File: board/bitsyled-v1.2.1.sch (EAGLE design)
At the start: 8 parts

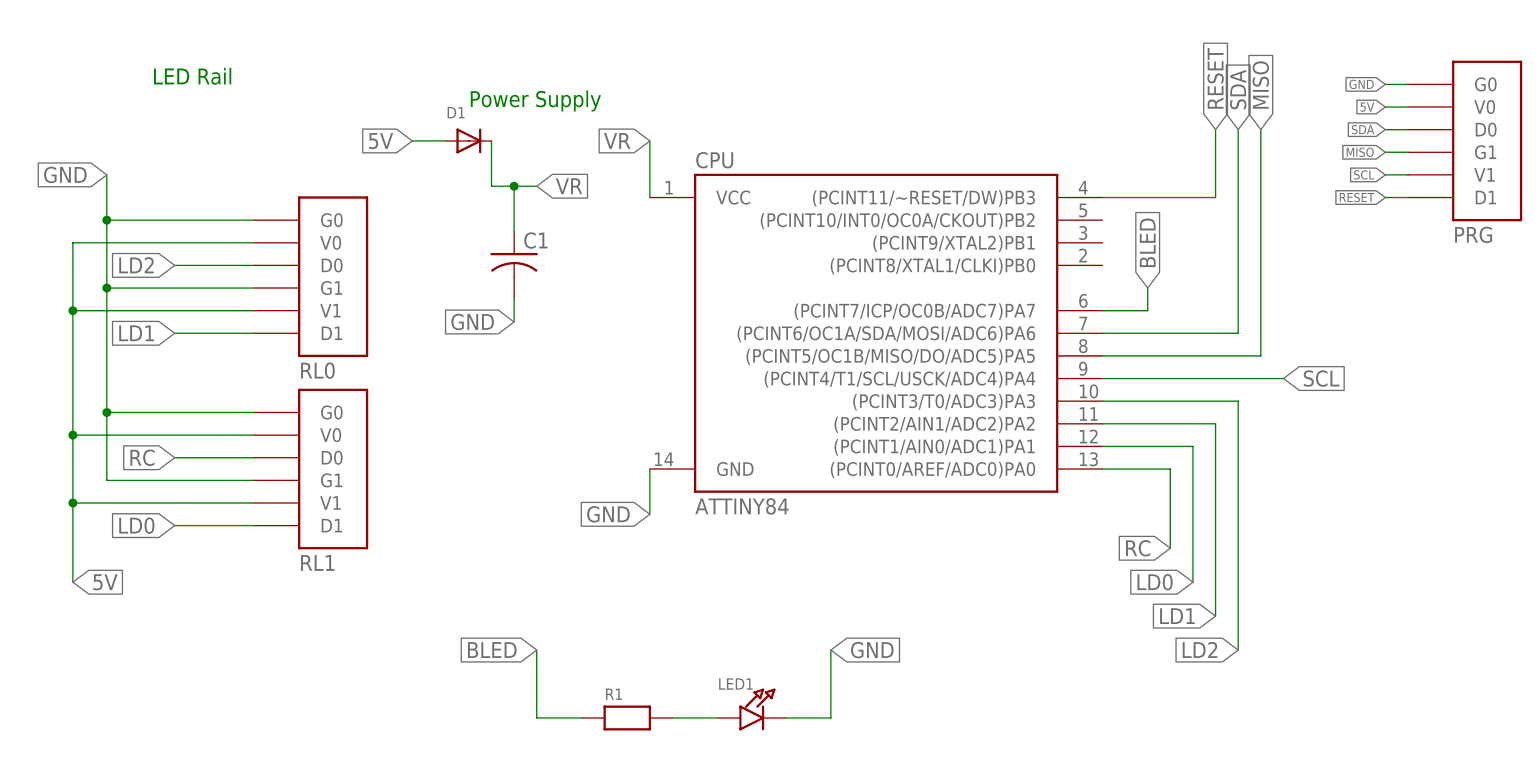
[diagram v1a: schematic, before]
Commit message: Adding presets
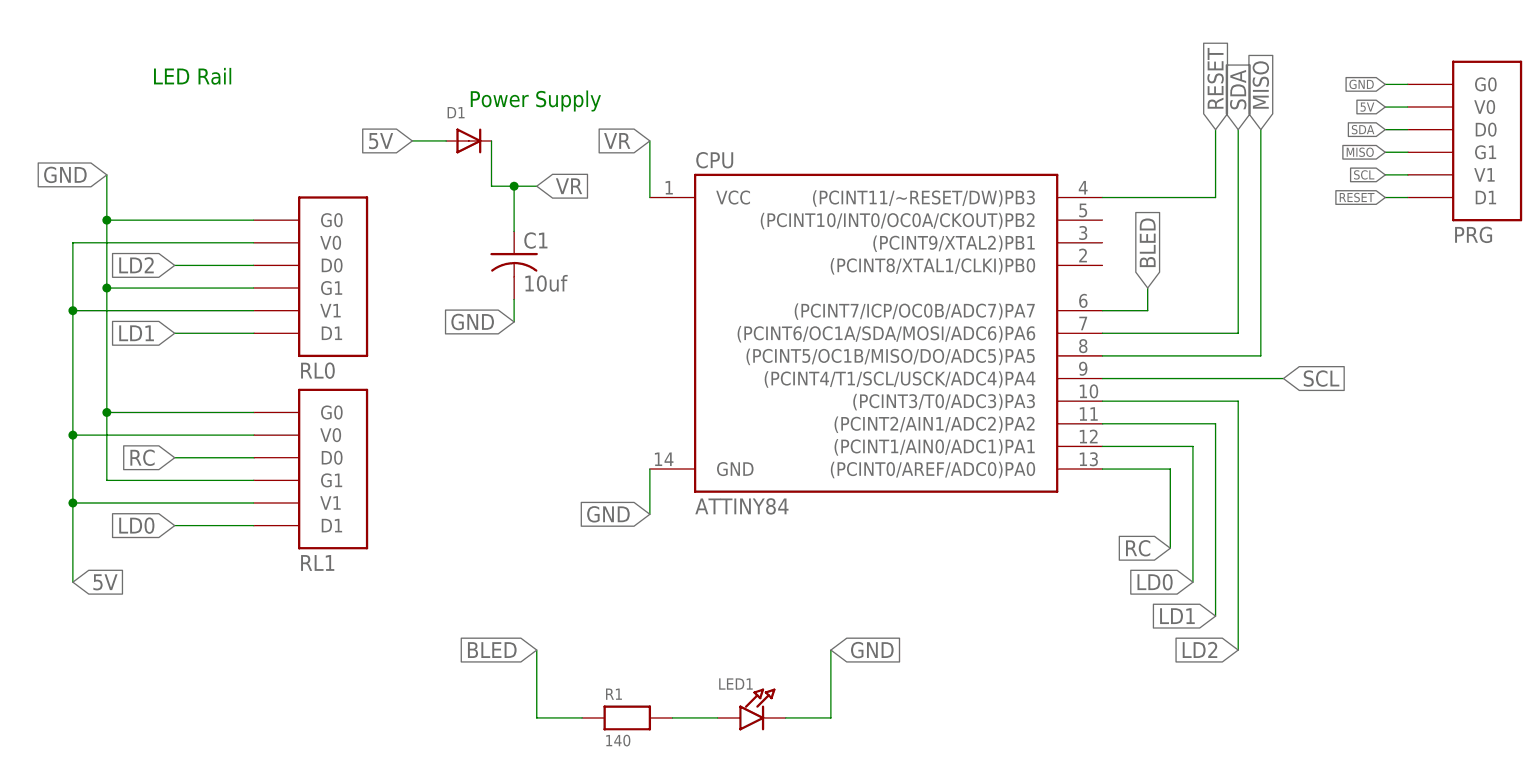
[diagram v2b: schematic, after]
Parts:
- C1: value (none) -> 10uf
- R1: value (none) -> 140
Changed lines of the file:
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@@
 <?xml version="1.0" encoding="utf-8"?>
 <!DOCTYPE eagle SYSTEM "eagle.dtd">
-<eagle version="8.3.2">
+<eagle version="9.3.2">
 <drawing>
 <settings>
@@
 <parts>
 <part name="CPU" library="SparkFun-IC-Microcontroller" deviceset="ATTINY84" device="" value="ATTINY84"/>
-<part name="C1" library="adafruit" deviceset="C-US" device="C0805"/>
+<part name="C1" library="adafruit" deviceset="C-US" device="C0805" value="10uf"/>
 <part name="D1" library="adafruit" deviceset="DIODE" device="SOD-123"/>
 <part name="LED1" library="microbuilder" deviceset="LED" device="0805_NOOUTLINE"/>
-<part name="R1" library="microbuilder" deviceset="RESISTOR" device="_0805"/>
+<part name="R1" library="microbuilder" deviceset="RESISTOR" device="_0805" value="140"/>
 <part name="RL0" library="FPVTools" deviceset="BITSYLED_1X6_RAIL" device="NORMAL"/>
 <part name="RL1" library="FPVTools" deviceset="BITSYLED_1X6_RAIL" device="REVERSED" value="BITSYLED_1X6_RAILREVERSED"/>
@@
 </plain>
 <instances>
-<instance part="CPU" gate="G$1" x="50.8" y="66.04"/>
-<instance part="C1" gate="G$1" x="10.16" y="74.93"/>
-<instance part="D1" gate="G$1" x="5.08" y="87.63"/>
-<instance part="LED1" gate="G$1" x="38.1" y="22.86"/>
-<instance part="R1" gate="G$1" x="22.86" y="22.86"/>
-<instance part="RL0" gate="G$1" x="-8.89" y="71.12"/>
-<instance part="RL1" gate="G$1" x="-8.89" y="49.53"/>
-<instance part="PRG" gate="G$1" x="120.65" y="86.36"/>
+<instance part="CPU" gate="G$1" x="50.8" y="66.04" smashed="yes">
+<attribute name="NAME" x="30.48" y="84.582" size="1.778" layer="95"/>
+<attribute name="VALUE" x="30.48" y="45.72" size="1.778" layer="96"/>
+</instance>
+<instance part="C1" gate="G$1" x="10.16" y="74.93" smashed="yes">
+<attribute name="NAME" x="11.176" y="75.565" size="1.778" layer="95"/>
+<attribute name="VALUE" x="11.176" y="70.739" size="1.778" layer="96"/>
+</instance>
+<instance part="D1" gate="G$1" x="5.08" y="87.63" smashed="yes">
+<attribute name="NAME" x="2.54" y="90.17" size="1.27" layer="95"/>
+<attribute name="VALUE" x="2.54" y="83.82" size="1.27" layer="96"/>
+</instance>
+<instance part="LED1" gate="G$1" x="38.1" y="22.86" smashed="yes">
+<attribute name="NAME" x="33.02" y="26.035" size="1.27" layer="95"/>
+<attribute name="VALUE" x="33.02" y="20.066" size="1.27" layer="96"/>
+</instance>
+<instance part="R1" gate="G$1" x="22.86" y="22.86" smashed="yes">
+<attribute name="NAME" x="20.32" y="24.892" size="1.27" layer="95" font="vector"/>
+<attribute name="VALUE" x="20.32" y="19.685" size="1.27" layer="96" font="vector"/>
+</instance>
+<instance part="RL0" gate="G$1" x="-8.89" y="71.12" smashed="yes">
+<attribute name="NAME" x="-13.97" y="60.96" size="1.778" layer="95"/>
+</instance>
+<instance part="RL1" gate="G$1" x="-8.89" y="49.53" smashed="yes">
+<attribute name="NAME" x="-13.97" y="39.37" size="1.778" layer="95"/>
+</instance>
+<instance part="PRG" gate="G$1" x="120.65" y="86.36" smashed="yes">
+<attribute name="NAME" x="115.57" y="76.2" size="1.778" layer="95"/>
+</instance>
 </instances>
 <busses>
